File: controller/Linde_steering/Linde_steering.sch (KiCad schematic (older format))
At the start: 21 parts, among them P1 CONN_01X06, P2 CONN_01X06, Q1 Q_NMOS_GDS, U1 LTV-827, U2 TL072

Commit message: Cleanup
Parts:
- D1, D2: value 6V8 -> BZX84V006.8; footprint Diodes_SMD:D_SMA_Handsoldering -> TO_SOT_Packages_SMD:SOT-23
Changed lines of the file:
@@
 P 8250 5550
 F 0 "D2" H 8250 5650 50  0000 C CNN
-F 1 "6V8" H 8250 5450 50  0000 C CNN
-F 2 "Diodes_SMD:D_SMA_Handsoldering" H 8250 5550 50  0000 C CNN
+F 1 "BZX84V006.8" H 8250 5450 50  0000 C CNN
+F 2 "TO_SOT_Packages_SMD:SOT-23" H 8250 5550 50  0000 C CNN
 F 3 "" H 8250 5550 50  0000 C CNN
 	1    8250 5550
@@
 P 8250 4200
 F 0 "D1" H 8250 4300 50  0000 C CNN
-F 1 "6V8" H 8250 4100 50  0000 C CNN
-F 2 "Diodes_SMD:D_SMA_Handsoldering" H 8250 4200 50  0000 C CNN
+F 1 "BZX84V006.8" H 8250 4100 50  0000 C CNN
+F 2 "TO_SOT_Packages_SMD:SOT-23" H 8250 4200 50  0001 C CNN
 F 3 "" H 8250 4200 50  0000 C CNN
 	1    8250 4200

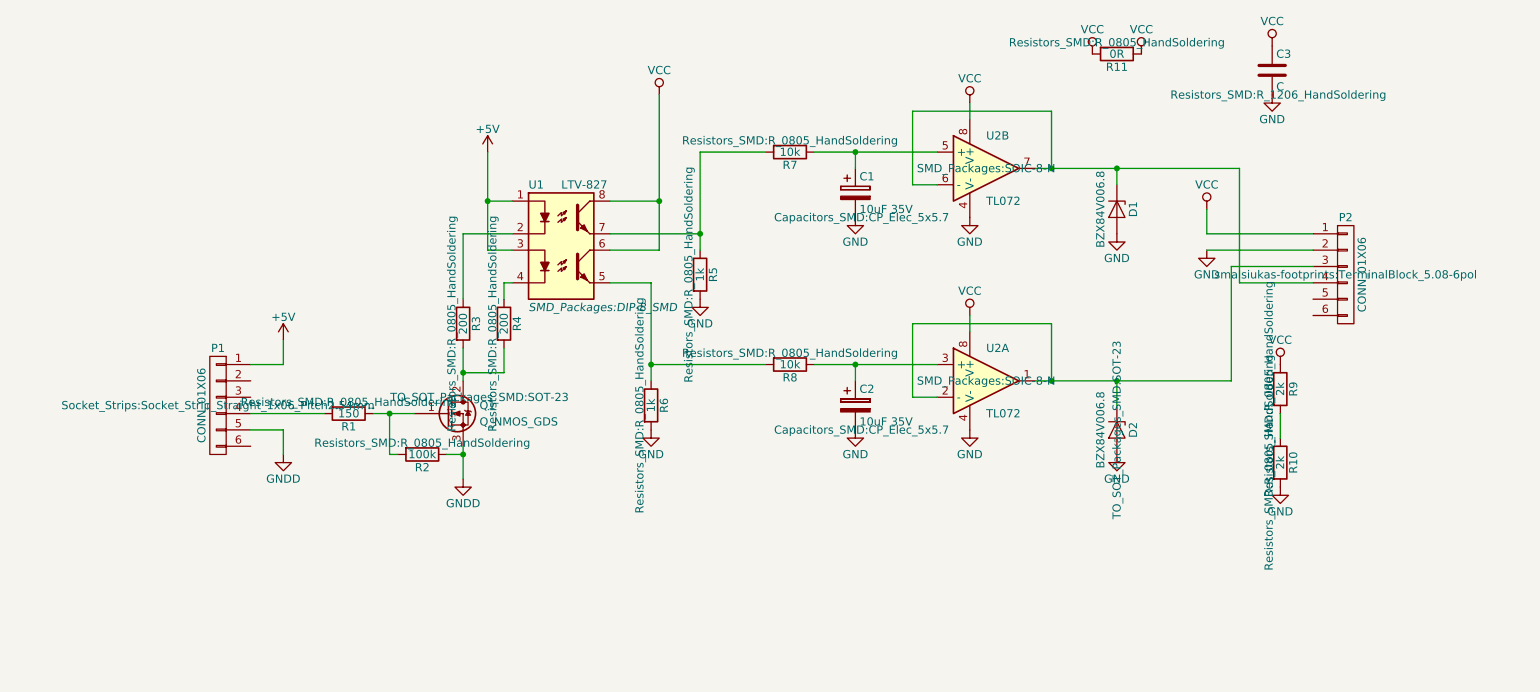
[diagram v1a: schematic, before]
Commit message: Mounting holes added
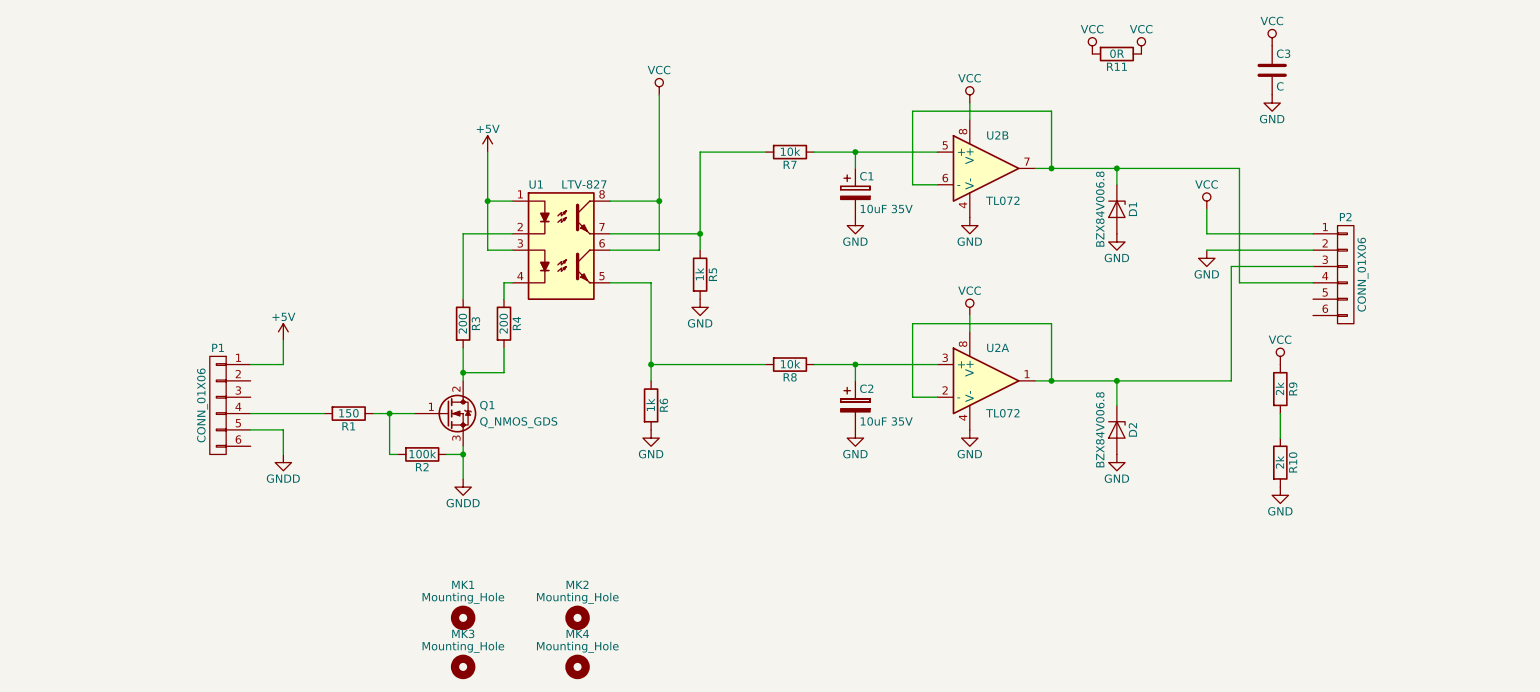
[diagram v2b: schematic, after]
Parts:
- removed D1, D2: BZX84V006.8, TO_SOT_Packages_SMD:SOT-23, symbol D_Zener
- added D1, D2: BZX84V006.8, TO_SOT_Packages_SMD:SOT-23, symbol Zener_BZX84
- added MK1, MK2, MK3, MK4: Mounting_Hole, Mounting_Holes:MountingHole_3.2mm_M3_Pad, symbol Mounting_Hole
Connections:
- net GND: now also D1.1 (A), D2.1 (A)
- net at P2.3 (P3), U2.1, U2.2 (-): now also D2.3 (K)
- net at P2.4 (P4), U2.6 (-), U2.7: now also D1.3 (K)
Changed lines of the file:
@@
 LIBS:contrib
 LIBS:valves
+LIBS:mechanical
+LIBS:zener_bzx84
 LIBS:Linde_steering-cache
 EELAYER 25 0
@@
 F 0 "U2" H 7450 5450 50  0000 L CNN
 F 1 "TL072" H 7450 5050 50  0000 L CNN
-F 2 "SMD_Packages:SOIC-8-N" H 7450 5250 50  0000 C CNN
+F 2 "SMD_Packages:SOIC-8-N" H 7450 5250 50  0001 C CNN
 F 3 "" H 7450 5250 50  0000 C CNN
 	1    7450 5250
@@
 F 0 "U2" H 7450 4150 50  0000 L CNN
 F 1 "TL072" H 7450 3750 50  0000 L CNN
-F 2 "SMD_Packages:SOIC-8-N" H 7450 3950 50  0000 C CNN
+F 2 "SMD_Packages:SOIC-8-N" H 7450 3950 50  0001 C CNN
 F 3 "" H 7450 3950 50  0000 C CNN
 	2    7450 3950
@@
 $EndComp
 $Comp
-L D_Zener D2
-U 1 1 58D11987
-P 8250 5550
-F 0 "D2" H 8250 5650 50  0000 C CNN
-F 1 "BZX84V006.8" H 8250 5450 50  0000 C CNN
-F 2 "TO_SOT_Packages_SMD:SOT-23" H 8250 5550 50  0000 C CNN
-F 3 "" H 8250 5550 50  0000 C CNN
-	1    8250 5550
-	0    1    1    0
-$EndComp
-$Comp
-L D_Zener D1
-U 1 1 58D119FC
-P 8250 4200
-F 0 "D1" H 8250 4300 50  0000 C CNN
-F 1 "BZX84V006.8" H 8250 4100 50  0000 C CNN
-F 2 "TO_SOT_Packages_SMD:SOT-23" H 8250 4200 50  0001 C CNN
-F 3 "" H 8250 4200 50  0000 C CNN
-	1    8250 4200
-	0    1    1    0
-$EndComp
-$Comp
 L GND #PWR05
 U 1 1 58D11A91
@@
 F 0 "P2" H 9650 4950 50  0000 C CNN
 F 1 "CONN_01X06" V 9750 4600 50  0000 C CNN
-F 2 "smalsiukas-footprints:TerminalBlock_5.08-6pol" H 9650 4600 50  0000 C CNN
+F 2 "smalsiukas-footprints:TerminalBlock_5.08-6pol" H 9650 4600 50  0001 C CNN
 F 3 "" H 9650 4600 50  0000 C CNN
 	1    9650 4600
@@
 F 0 "C1" H 6675 4200 50  0000 L CNN
 F 1 "10uF 35V" H 6675 4000 50  0000 L CNN
-F 2 "Capacitors_SMD:CP_Elec_5x5.7" H 6688 3950 50  0000 C CNN
+F 2 "Capacitors_SMD:CP_Elec_5x5.7" H 6688 3950 50  0001 C CNN
 F 3 "" H 6650 4100 50  0000 C CNN
 	1    6650 4100
@@
 F 0 "C2" H 6675 5500 50  0000 L CNN
 F 1 "10uF 35V" H 6675 5300 50  0000 L CNN
-F 2 "Capacitors_SMD:CP_Elec_5x5.7" H 6688 5250 50  0000 C CNN
+F 2 "Capacitors_SMD:CP_Elec_5x5.7" H 6688 5250 50  0001 C CNN
 F 3 "" H 6650 5400 50  0000 C CNN
 	1    6650 5400
@@
 F 0 "R7" V 6330 3850 50  0000 C CNN
 F 1 "10k" V 6250 3850 50  0000 C CNN
-F 2 "Resistors_SMD:R_0805_HandSoldering" V 6180 3850 50  0000 C CNN
+F 2 "Resistors_SMD:R_0805_HandSoldering" V 6180 3850 50  0001 C CNN
 F 3 "" H 6250 3850 50  0000 C CNN
 	1    6250 3850
@@
 F 0 "R8" V 6330 5150 50  0000 C CNN
 F 1 "10k" V 6250 5150 50  0000 C CNN
-F 2 "Resistors_SMD:R_0805_HandSoldering" V 6180 5150 50  0000 C CNN
+F 2 "Resistors_SMD:R_0805_HandSoldering" V 6180 5150 50  0001 C CNN
 F 3 "" H 6250 5150 50  0000 C CNN
 	1    6250 5150
@@
 F 0 "U1" H 4650 4850 50  0000 L CNN
 F 1 "LTV-827" H 4850 4850 50  0000 L CNN
-F 2 "SMD_Packages:DIP-8_SMD" H 4650 4100 50  0000 L CIN
+F 2 "SMD_Packages:DIP-8_SMD" H 4650 4100 50  0001 L CIN
 F 3 "" H 4850 4350 50  0000 L CNN
 	1    4850 4450
@@
 F 0 "R5" V 5780 4600 50  0000 C CNN
 F 1 "1k" V 5700 4600 50  0000 C CNN
-F 2 "Resistors_SMD:R_0805_HandSoldering" V 5630 4600 50  0000 C CNN
+F 2 "Resistors_SMD:R_0805_HandSoldering" V 5630 4600 50  0001 C CNN
 F 3 "" H 5700 4600 50  0000 C CNN
 	1    5700 4600
@@
 F 0 "R6" V 5480 5400 50  0000 C CNN
 F 1 "1k" V 5400 5400 50  0000 C CNN
-F 2 "Resistors_SMD:R_0805_HandSoldering" V 5330 5400 50  0000 C CNN
+F 2 "Resistors_SMD:R_0805_HandSoldering" V 5330 5400 50  0001 C CNN
 F 3 "" H 5400 5400 50  0000 C CNN
 	1    5400 5400
@@
 F 0 "R10" V 9330 5750 50  0000 C CNN
 F 1 "2k" V 9250 5750 50  0000 C CNN
-F 2 "Resistors_SMD:R_0805_HandSoldering" V 9180 5750 50  0000 C CNN
+F 2 "Resistors_SMD:R_0805_HandSoldering" V 9180 5750 50  0001 C CNN
 F 3 "" H 9250 5750 50  0000 C CNN
 	1    9250 5750
@@
 F 0 "R9" V 9330 5300 50  0000 C CNN
 F 1 "2k" V 9250 5300 50  0000 C CNN
-F 2 "Resistors_SMD:R_0805_HandSoldering" V 9180 5300 50  0000 C CNN
+F 2 "Resistors_SMD:R_0805_HandSoldering" V 9180 5300 50  0001 C CNN
 F 3 "" H 9250 5300 50  0000 C CNN
 	1    9250 5300
@@
 F 0 "R4" V 4580 4900 50  0000 C CNN
 F 1 "200" V 4500 4900 50  0000 C CNN
-F 2 "Resistors_SMD:R_0805_HandSoldering" V 4430 4900 50  0000 C CNN
+F 2 "Resistors_SMD:R_0805_HandSoldering" V 4430 4900 50  0001 C CNN
 F 3 "" H 4500 4900 50  0000 C CNN
 	1    4500 4900
@@
 F 0 "R3" V 4330 4900 50  0000 C CNN
 F 1 "200" V 4250 4900 50  0000 C CNN
-F 2 "Resistors_SMD:R_0805_HandSoldering" V 4180 4900 50  0000 C CNN
+F 2 "Resistors_SMD:R_0805_HandSoldering" V 4180 4900 50  0001 C CNN
 F 3 "" H 4250 4900 50  0000 C CNN
 	1    4250 4900
@@
 F 0 "P1" H 2750 5750 50  0000 C CNN
 F 1 "CONN_01X06" V 2850 5400 50  0000 C CNN
-F 2 "Socket_Strips:Socket_Strip_Straight_1x06_Pitch2.54mm" H 2750 5400 50  0000 C CNN
+F 2 "Socket_Strips:Socket_Strip_Straight_1x06_Pitch2.54mm" H 2750 5400 50  0001 C CNN
 F 3 "" H 2750 5400 50  0000 C CNN
 	1    2750 5400
@@
 F 0 "C3" H 9225 3450 50  0000 L CNN
 F 1 "C" H 9225 3250 50  0000 L CNN
-F 2 "Resistors_SMD:R_1206_HandSoldering" H 9238 3200 50  0000 C CNN
+F 2 "Resistors_SMD:R_1206_HandSoldering" H 9238 3200 50  0001 C CNN
 F 3 "" H 9200 3350 50  0000 C CNN
 	1    9200 3350
@@
 F 0 "Q1" H 4350 5500 50  0000 L CNN
 F 1 "Q_NMOS_GDS" H 4350 5400 50  0000 L CNN
-F 2 "TO_SOT_Packages_SMD:SOT-23" H 4350 5550 50  0000 C CNN
+F 2 "TO_SOT_Packages_SMD:SOT-23" H 4350 5550 50  0001 C CNN
 F 3 "" H 4150 5450 50  0000 C CNN
 	1    4150 5450
@@
 F 0 "R1" V 3630 5450 50  0000 C CNN
 F 1 "150" V 3550 5450 50  0000 C CNN
-F 2 "Resistors_SMD:R_0805_HandSoldering" V 3480 5450 50  0000 C CNN
+F 2 "Resistors_SMD:R_0805_HandSoldering" V 3480 5450 50  0001 C CNN
 F 3 "" H 3550 5450 50  0000 C CNN
 	1    3550 5450
@@
 F 0 "R2" V 4080 5700 50  0000 C CNN
 F 1 "100k" V 4000 5700 50  0000 C CNN
-F 2 "Resistors_SMD:R_0805_HandSoldering" V 3930 5700 50  0000 C CNN
+F 2 "Resistors_SMD:R_0805_HandSoldering" V 3930 5700 50  0001 C CNN
 F 3 "" H 4000 5700 50  0000 C CNN
 	1    4000 5700
@@
 F 0 "R11" V 8330 3250 50  0000 C CNN
 F 1 "0R" V 8250 3250 50  0000 C CNN
-F 2 "Resistors_SMD:R_0805_HandSoldering" V 8180 3250 50  0000 C CNN
+F 2 "Resistors_SMD:R_0805_HandSoldering" V 8180 3250 50  0001 C CNN
 F 3 "" H 8250 3250 50  0000 C CNN
 	1    8250 3250
@@
 	1    0    0    -1
 $EndComp
+$Comp
+L Mounting_Hole MK1
+U 1 1 58D0DFD3
+P 4250 6700
+F 0 "MK1" H 4250 6900 50  0000 C CNN
+F 1 "Mounting_Hole" H 4250 6825 50  0000 C CNN
+F 2 "Mounting_Holes:MountingHole_3.2mm_M3_Pad" H 4250 6700 60  0001 C CNN
+F 3 "" H 4250 6700 60  0001 C CNN
+	1    4250 6700
+	1    0    0    -1
+$EndComp
+$Comp
+L Mounting_Hole MK3
+U 1 1 58D0E186
+P 4250 7000
+F 0 "MK3" H 4250 7200 50  0000 C CNN
+F 1 "Mounting_Hole" H 4250 7125 50  0000 C CNN
+F 2 "Mounting_Holes:MountingHole_3.2mm_M3_Pad" H 4250 7000 60  0001 C CNN
+F 3 "" H 4250 7000 60  0001 C CNN
+	1    4250 7000
+	1    0    0    -1
+$EndComp
+$Comp
+L Mounting_Hole MK2
+U 1 1 58D0E1E6
+P 4950 6700
+F 0 "MK2" H 4950 6900 50  0000 C CNN
+F 1 "Mounting_Hole" H 4950 6825 50  0000 C CNN
+F 2 "Mounting_Holes:MountingHole_3.2mm_M3_Pad" H 4950 6700 60  0001 C CNN
+F 3 "" H 4950 6700 60  0001 C CNN
+	1    4950 6700
+	1    0    0    -1
+$EndComp
+$Comp
+L Mounting_Hole MK4
+U 1 1 58D0E257
+P 4950 7000
+F 0 "MK4" H 4950 7200 50  0000 C CNN
+F 1 "Mounting_Hole" H 4950 7125 50  0000 C CNN
+F 2 "Mounting_Holes:MountingHole_3.2mm_M3_Pad" H 4950 7000 60  0001 C CNN
+F 3 "" H 4950 7000 60  0001 C CNN
+	1    4950 7000
+	1    0    0    -1
+$EndComp
+$Comp
+L Zener_BZX84 D2
+U 1 1 58D0F5BD
+P 8250 5550
+F 0 "D2" H 8250 5650 50  0000 C CNN
+F 1 "BZX84V006.8" H 8250 5450 50  0000 C CNN
+F 2 "TO_SOT_Packages_SMD:SOT-23" H 8250 5550 50  0001 C CNN
+F 3 "" H 8250 5550 50  0000 C CNN
+	1    8250 5550
+	0    1    1    0
+$EndComp
+$Comp
+L Zener_BZX84 D1
+U 1 1 58D0FA90
+P 8250 4200
+F 0 "D1" H 8250 4300 50  0000 C CNN
+F 1 "BZX84V006.8" H 8250 4100 50  0000 C CNN
+F 2 "TO_SOT_Packages_SMD:SOT-23" H 8250 4200 50  0001 C CNN
+F 3 "" H 8250 4200 50  0000 C CNN
+	1    8250 4200
+	0    1    1    0
+$EndComp
 $EndSCHEMATC

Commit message: Cleanup
SMT GDS FET changed to more common GSD FET;
OSHW and CC symbols added to copper layer;
Gerbers updated and sent for manufacturing;

Typeo fixed in Arduino code
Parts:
- removed Q1: Q_NMOS_GDS, TO_SOT_Packages_SMD:SOT-23, symbol Q_NMOS_GDS
- added Q1: Q_NMOS_GSD, symbol Q_NMOS_GSD
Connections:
- net GNDD: now also Q1.2 (S)
- net at R3.2, R4.2: now also Q1.3 (D)
- net at R1.1, R2.2: now also Q1.1 (G)
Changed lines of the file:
@@
-	1    0    0    -1
-$EndComp
-$Comp
-L Q_NMOS_GDS Q1
-U 1 1 58D15D9E
-P 4150 5450
-F 0 "Q1" H 4350 5500 50  0000 L CNN
-F 1 "Q_NMOS_GDS" H 4350 5400 50  0000 L CNN
-F 2 "TO_SOT_Packages_SMD:SOT-23" H 4350 5550 50  0001 C CNN
-F 3 "" H 4150 5450 50  0000 C CNN
-	1    4150 5450
 	1    0    0    -1
 $EndComp
@@
 	0    1    1    0
 $EndComp
+$Comp
+L Q_NMOS_GSD Q1
+U 1 1 58D3B817
+P 4150 5450
+F 0 "Q1" H 4350 5500 50  0000 L CNN
+F 1 "Q_NMOS_GSD" H 4350 5400 50  0000 L CNN
+F 2 "" H 4350 5550 50  0000 C CNN
+F 3 "" H 4150 5450 50  0000 C CNN
+	1    4150 5450
+	1    0    0    -1
+$EndComp
 $EndSCHEMATC
